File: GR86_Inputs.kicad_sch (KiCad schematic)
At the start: 34 parts, among them CN3 SM05B-SURS-TF(LF)(SN), U10 74LVC1G14, U11 74LVC1G14, U12 74LVC1G14, U7 74LVC1G14, U8 74LVC1G14, U9 74LVC1G14

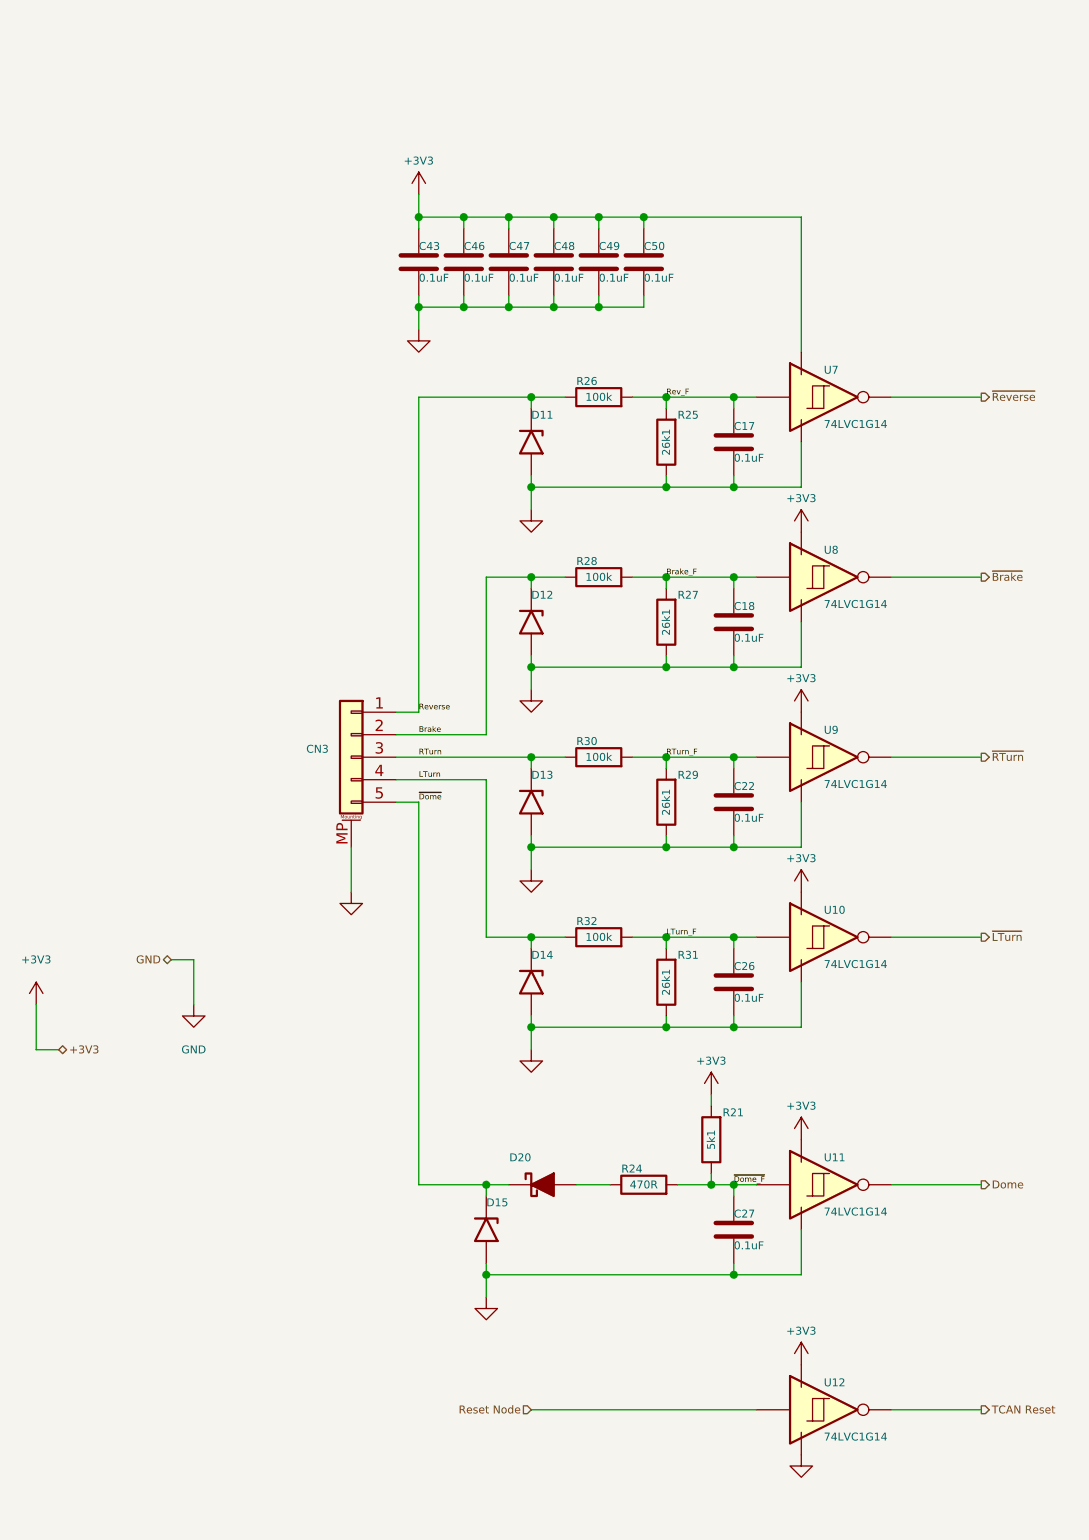
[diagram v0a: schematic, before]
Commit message: Update CANBus_Interface.kicad_sch, ESP32-S3 D1 Pico Board.kicad_sch, ESP32-S3 Pico D1.kicad_pcb, and 15 more files
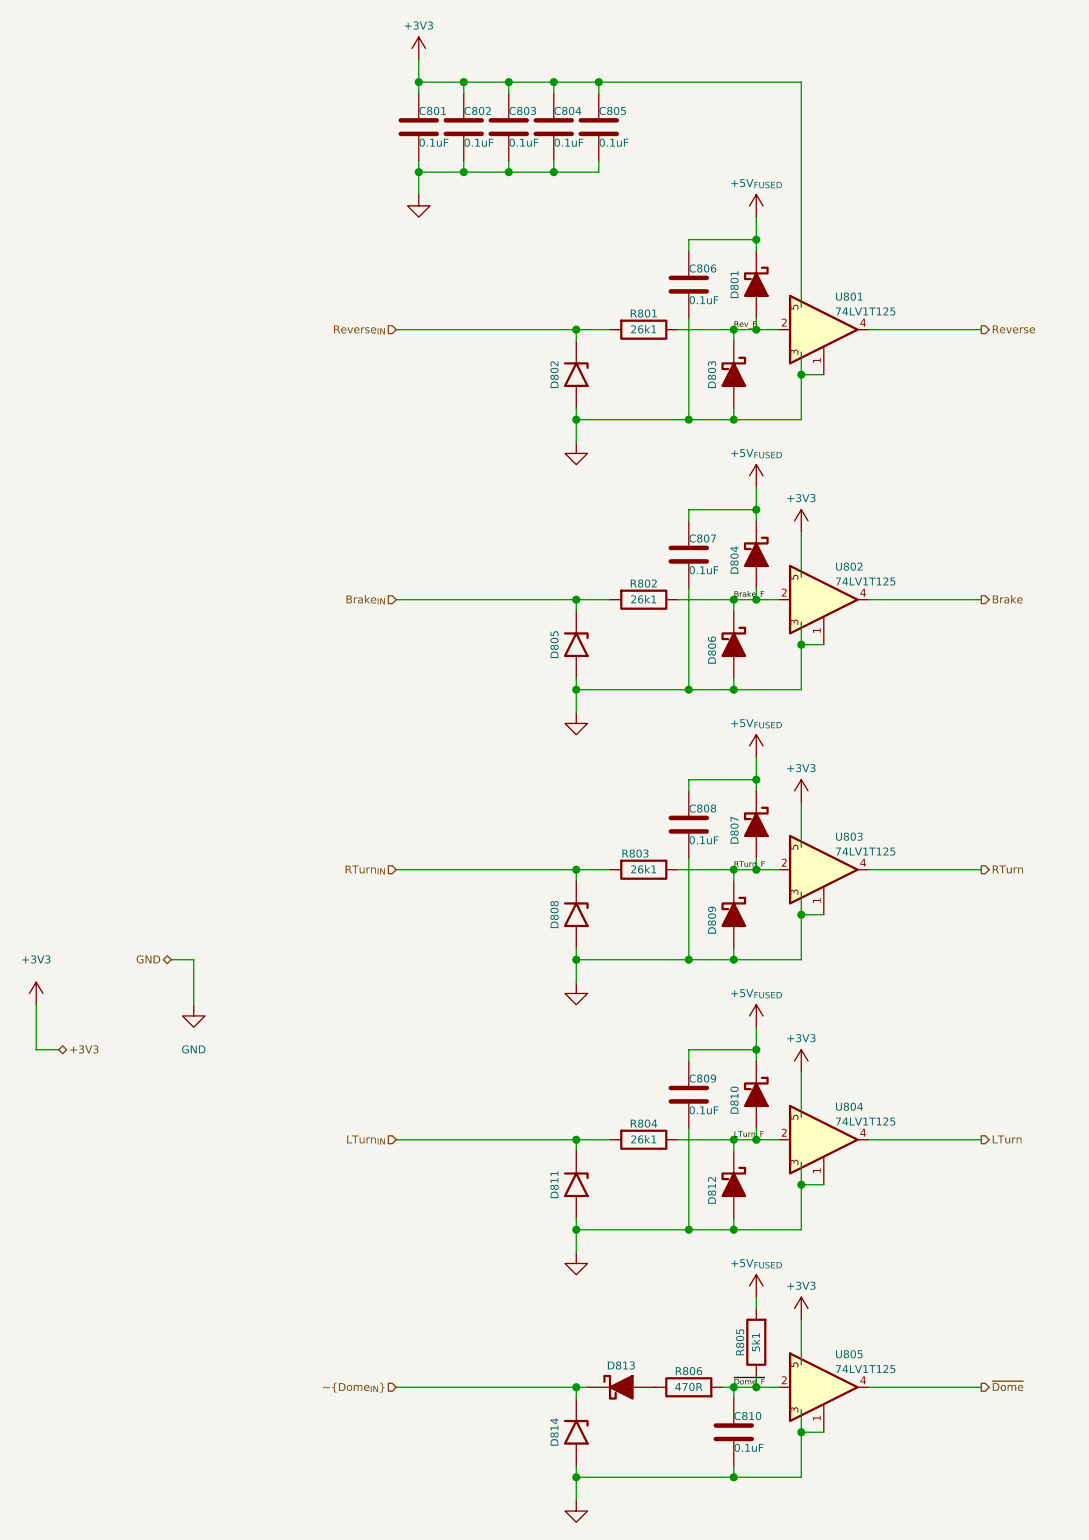
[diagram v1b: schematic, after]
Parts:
- removed C18, C22, C26, C50: 0.1uF, Capacitors:C_0201_Dense, symbol Device:C
- removed CN3: SM05B-SURS-TF(LF)(SN), Personal_FootprintLibrary:JST_SUH_1x05_MP_P0.8mm, symbol PersonalSchematicSymbolLibrary:Conn_01x05_MountingPin
- removed D12, D13, D14: D15V0H1U2LP-7B, Personal_FootprintLibrary:DFN1006-2, symbol PersonalSchematicSymbolLibrary:TVS_Unidirectional
- removed R26, R28, R30, R32: 100k, Resistors:R_0201_Dense, symbol Device:R
- removed R27, R29, R31: 26k1, Resistors:R_0201_Dense, symbol Device:R
- removed U10, U11, U12, U7, U8, U9: 74LVC1G14, Personal_FootprintLibrary:X2SON5_SOT1226_0.8x0.8mm, symbol 74xxx1Gyy:74LVC1G14
- added C807, C808, C809: 0.1uF, My Capacitors:C_0201_Dense, symbol Device:C
- added D801, D803, D804, D806, D807, D809, D810, D812: PMEG4002ESFYL, Personal_FootprintLibrary:DSN0603-2, symbol PersonalSchematicSymbolLibrary:D_Schottky_Filled
- added D805, D808, D811: D15V0H1U2LP-7B, Personal_FootprintLibrary:DFN1006-2, symbol PersonalSchematicSymbolLibrary:TVS_Unidirectional
- added R802, R803, R804: 26k1, My Resistors:R_0201_Dense, symbol Device:R
- added U801, U802, U803, U804, U805: 74LV1T125, Personal_FootprintLibrary:X2SON5_SOT1226_0.8x0.8mm, symbol 74xxx1Gyy:74LVC1G125
- C801: renamed from C43; footprint Capacitors:C_0201_Dense -> My Capacitors:C_0201_Dense
- C802: renamed from C46; footprint Capacitors:C_0201_Dense -> My Capacitors:C_0201_Dense
- C803: renamed from C47; footprint Capacitors:C_0201_Dense -> My Capacitors:C_0201_Dense
- C804: renamed from C48; footprint Capacitors:C_0201_Dense -> My Capacitors:C_0201_Dense
- C805: renamed from C49; footprint Capacitors:C_0201_Dense -> My Capacitors:C_0201_Dense
- C806: renamed from C17; footprint Capacitors:C_0201_Dense -> My Capacitors:C_0201_Dense
- C810: renamed from C27; footprint Capacitors:C_0201_Dense -> My Capacitors:C_0201_Dense
- D813: renamed from D20; value SDM1100LP-7 -> PMEG4002ESFYL; footprint Personal_FootprintLibrary:DFN2020-2 -> Personal_FootprintLibrary:DSN0603-2; Distributor Link 1 https://www.digikey.com/en/products/detail/diodes-incorpora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 -> https://www.digikey.com/en/products/detail/nexperia-usa-inc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; Distributor Link 2 https://www.mouser.com/ProductDetail/Diodes-Incorporated/SD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 -> https://www.mouser.com/ProductDetail/Nexperia/PMEG4002ESFYL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; LCSC C6999905 -> C22435168; Manufacturer Diodes Incorporated -> Nexperia USA Inc.; Manufacturer Part Number SDM1100LP-7 -> PMEG4002ESFYL
- R801: renamed from R25; footprint Resistors:R_0201_Dense -> My Resistors:R_0201_Dense
- R805: renamed from R21; footprint Resistors:R_0201_Dense -> My Resistors:R_0201_Dense
- R806: renamed from R24; footprint Resistors:R_0201_Dense -> My Resistors:R_0201_Dense
- renumbered D11 to D802, D15 to D814
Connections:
- net +3V3: now also U801.5 (VCC), U802.5 (VCC), U803.5 (VCC), U804.5 (VCC), U805.5 (VCC); no longer R805.2
- net Brake: now also U802.4 (Y)
- net Brake_F: now also D804.2 (A), D806.1 (K), R802.1, U802.2 (A)
- net GND: now also C807.2, C808.2, C809.2, D803.2 (A), D805.2 (A), D806.2 (A), D808.2 (A), D809.2 (A), D811.2 (A), D812.2 (A), U801.1 (OE), U801.3 (GND), U802.1 (OE), U802.3 (GND), U803.1 (OE), U803.3 (GND), U804.1 (OE), U804.3 (GND), U805.1 (OE), U805.3 (GND); no longer R801.1
- net LTurn: now also U804.4 (Y)
- net LTurn_F: now also D810.2 (A), D812.1 (K), R804.1, U804.2 (A)
- net RTurn: now also U803.4 (Y)
- net RTurn_F: now also D807.2 (A), D809.1 (K), R803.1, U803.2 (A)
- net Rev_F: now also R801.1, D801.2 (A), D803.1 (K), U801.2 (A); no longer C806.1, R801.2
- net Reverse: now also U801.4 (Y); no longer D802.1 (K)
- net ~{Dome_F}: now also U805.2 (A)
- net ~{Dome}: now also U805.4 (Y); no longer D813.1 (K), D814.1 (K)
- new net +5V_{FUSED}: C806.1, C807.1, C808.1, C809.1, D801.1 (K), D804.1 (K), D807.1 (K), D810.1 (K), R805.2
- new net Brake_{IN}: D805.1 (K), R802.2
- new net LTurn_{IN}: D811.1 (K), R804.2
- new net RTurn_{IN}: D808.1 (K), R803.2
- new net Reverse_{IN}: D802.1 (K), R801.2
- new net ~{Dome_{IN}}: D813.1 (K), D814.1 (K)
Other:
- moved on the sheet: C801, C802, C803, C804, C805, C806, C810, D802, D813, D814, R801, R805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
